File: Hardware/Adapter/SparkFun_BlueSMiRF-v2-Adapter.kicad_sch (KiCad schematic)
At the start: 3 parts, among them J1 JST_Locking_6, J2 Conn_01x06, J3 Conn_01x06

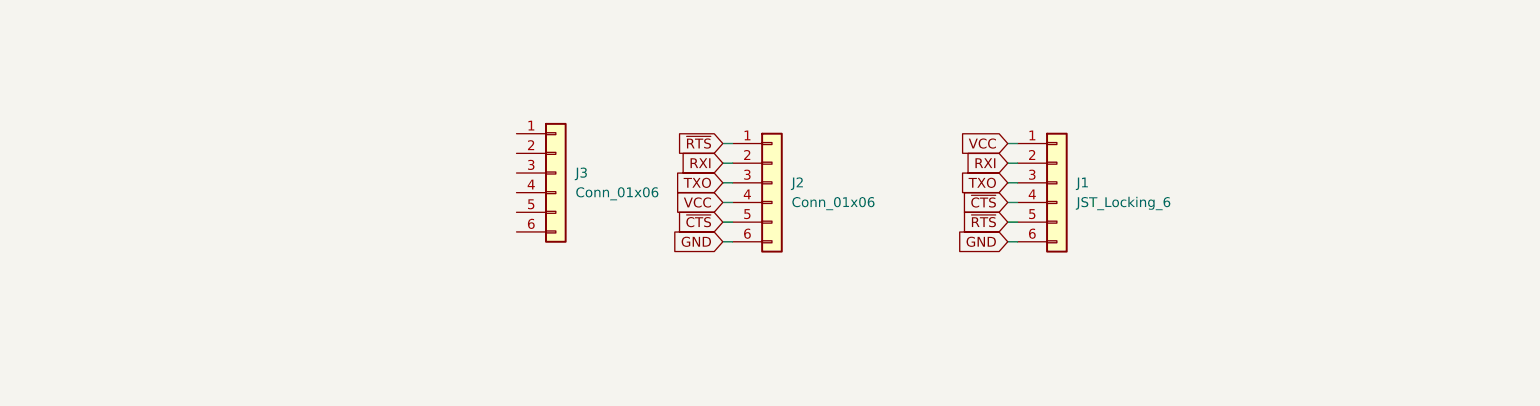
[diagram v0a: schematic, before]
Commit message: Make backwards compatible
Earlier boards had RX and TX lines swapped
- Adds switches on RX/TX lines
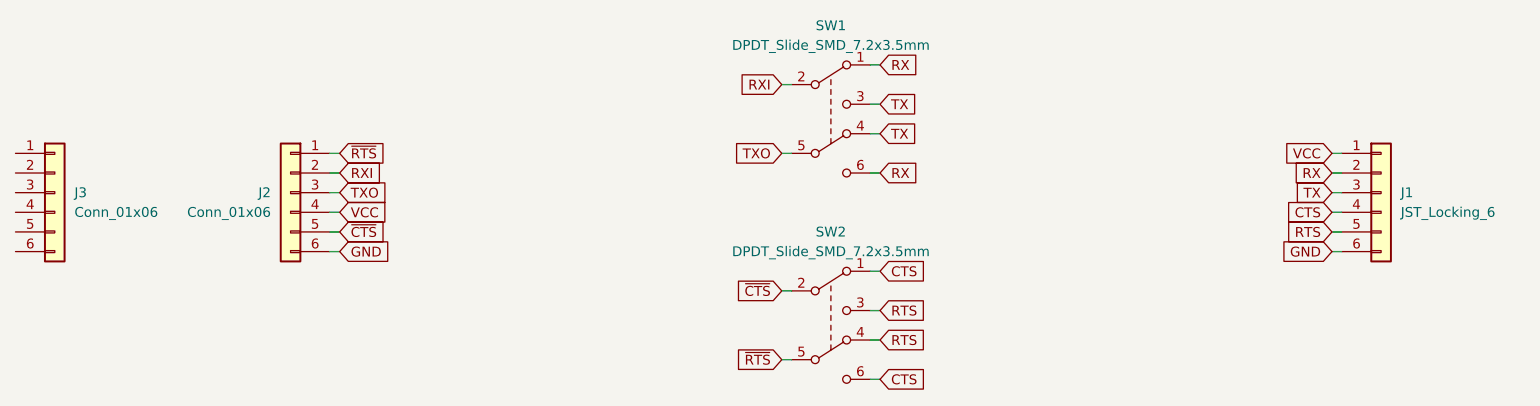
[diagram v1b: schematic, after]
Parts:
- added SW1, SW2: DPDT_Slide_SMD_7.2x3.5mm, SparkFun-Switch:Slide_DPDT_SMD_7.2x3.5mm, symbol SparkFun-Switch:DPDT_Slide_SMD_7.2x3.5mm
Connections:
- net RXI: now also SW1.2 (B); no longer J1.2 (Pin_2)
- net TXO: now also SW1.5 (B); no longer J1.3 (Pin_3)
- net ~{CTS}: now also SW2.2 (B); no longer J1.4 (Pin_4)
- net ~{RTS}: now also SW2.5 (B); no longer J1.5 (Pin_5)
- new net CTS: J1.4 (Pin_4), SW2.1 (A), SW2.6 (C)
- new net RTS: J1.5 (Pin_5), SW2.3 (C), SW2.4 (A)
- new net RX: J1.2 (Pin_2), SW1.1 (A), SW1.6 (C)
- new net TX: J1.3 (Pin_3), SW1.3 (C), SW1.4 (A)
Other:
- moved on the sheet: J1, J2, J3
